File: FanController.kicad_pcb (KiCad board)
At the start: 2 copper layers, 80 x 45 mm, 28 parts, among them J1 Conn_01x02_Female, J2 Conn_01x03_Male, J3 Conn_01x03_Male, J4 Conn_01x03_Male, J5 Conn_01x03_Male, Q1 AO3400A, Q2 AO3400A, Q3 AO3400A, Q4 AO3400A, U1 D-SUN-MP1584EN, U2 mh-et-live-minikit

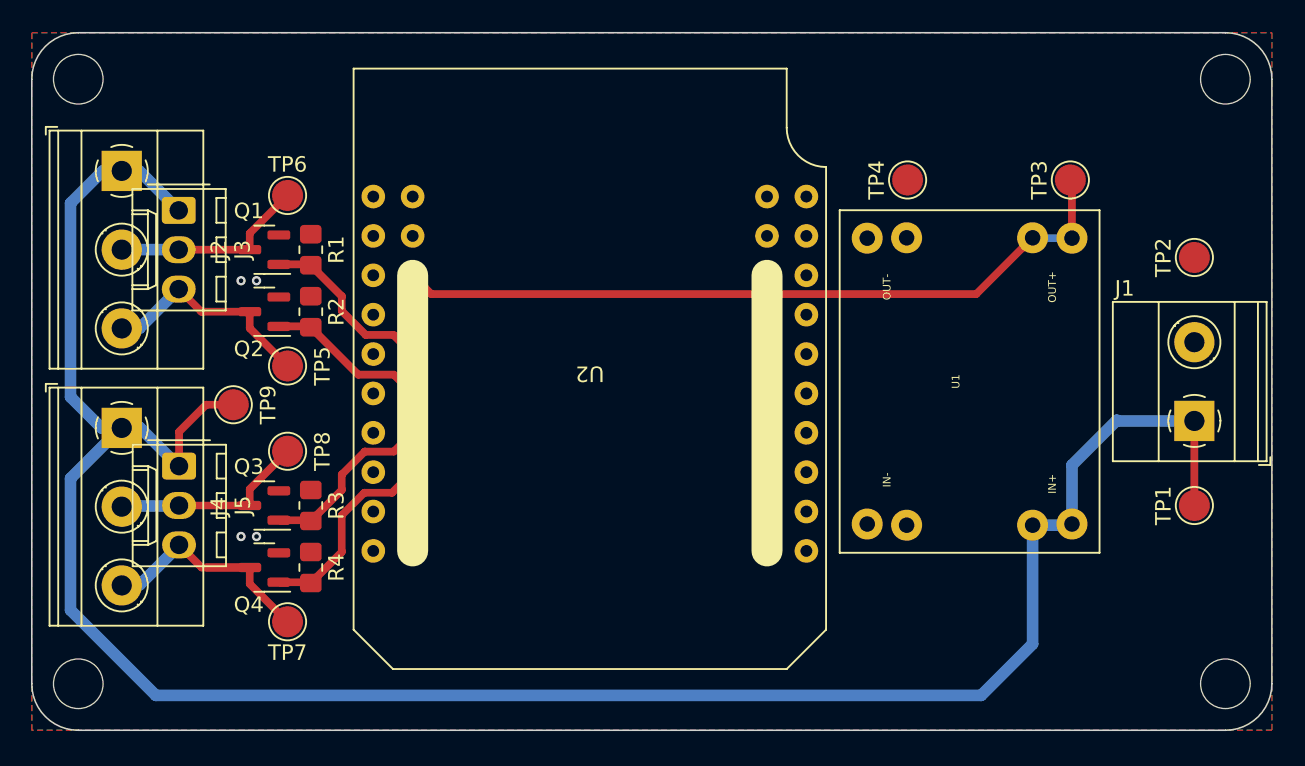
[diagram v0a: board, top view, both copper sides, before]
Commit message: shrinked board
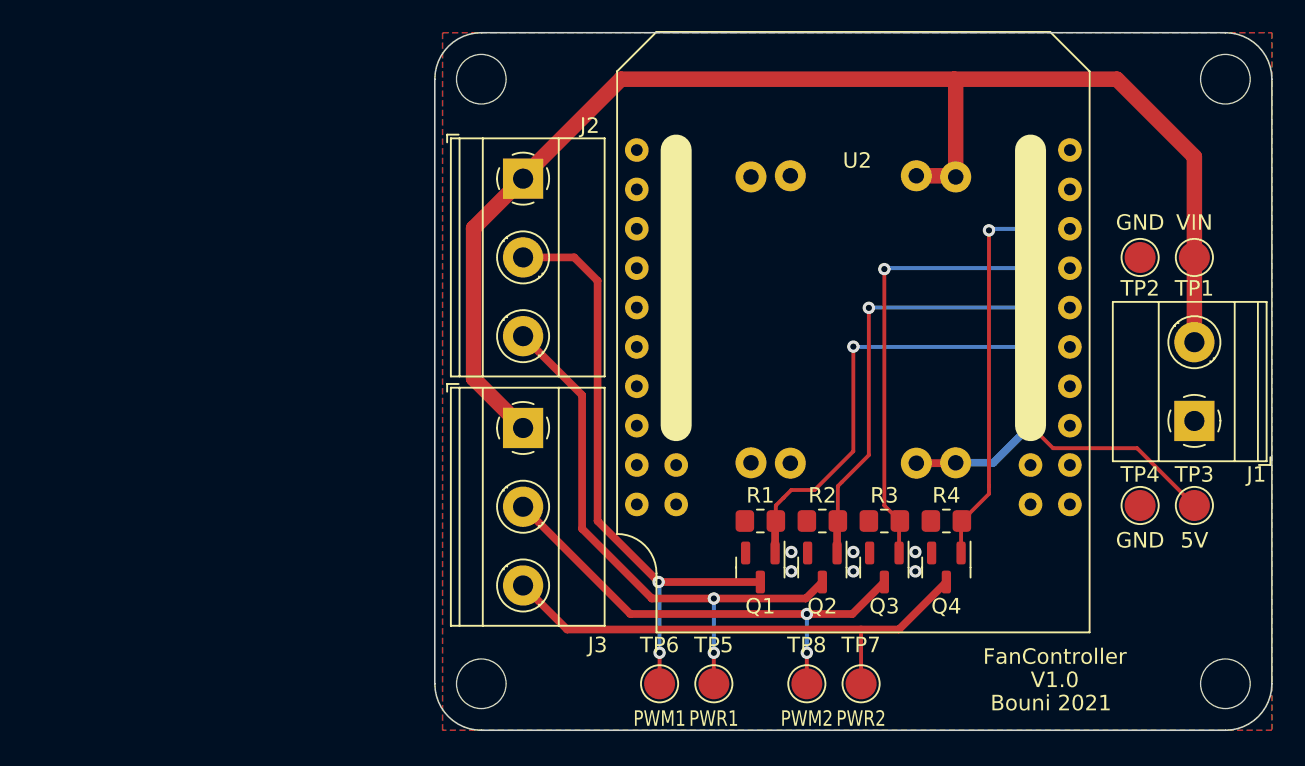
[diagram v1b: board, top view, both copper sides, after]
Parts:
- removed the J3 at (49.5, 41.5)
- removed J5: Conn_01x03_Male, Connector_Molex:Molex_KK-254_AE-6410-03A_1x03_P2.54mm_Vertical
- removed TP9: TestPoint, TestPoint:TestPoint_Pad_D2.0mm
- U1: moved to B.Cu
- moved Q4 44.0 mm to (99.0, 64.5), turned to -90 degrees
- moved R4 41.1 mm to (99.0, 61.5), turned to 0 degrees
- moved Q3 40.2 mm to (95.0, 64.5), turned to -90 degrees
- moved Q2 39.6 mm to (91.0, 64.5), turned to -90 degrees
- moved TP6 39.6 mm to (80.5, 72.0), turned to 180 degrees
- moved Q1 38.0 mm to (87.0, 64.5), turned to -90 degrees
- moved TP7 37.2 mm to (93.5, 72.0)
- moved R3 37.0 mm to (95.0, 61.5), turned to 0 degrees
- moved TP8 36.7 mm to (90.0, 72.0), turned to -90 degrees
- moved R2 35.7 mm to (91.0, 61.5), turned to 0 degrees
- moved TP5 34.3 mm to (84.0, 72.0), turned to 90 degrees
- moved R1 33.9 mm to (87.0, 61.5), turned to 0 degrees
- moved H1 26.0 mm to (69.0, 72.0)
- moved H2 26.0 mm to (69.0, 33.0)
- moved J2 25.9 mm to (71.7, 39.4)
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- renumbered J4 to J3
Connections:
- J1 pad 1: +12V -> GND
- J1 pad 2: GND -> +12V
- U2 pad 10: unconnected-(U2-Pad10) -> (no net)
- U2 pad 11: unconnected-(U2-Pad11) -> (no net)
- U2 pad 12: unconnected-(U2-Pad12) -> (no net)
- U2 pad 13: unconnected-(U2-Pad13) -> (no net)
- U2 pad 14: unconnected-(U2-Pad14) -> (no net)
- U2 pad 15: unconnected-(U2-Pad15) -> (no net)
- U2 pad 16: unconnected-(U2-Pad16) -> (no net)
- U2 pad 17: unconnected-(U2-Pad17) -> (no net)
- U2 pad 18: unconnected-(U2-Pad18) -> (no net)
- U2 pad 19: unconnected-(U2-Pad19) -> (no net)
- U2 pad 2: unconnected-(U2-Pad2) -> (no net)
- U2 pad 20: unconnected-(U2-Pad20) -> (no net)
- U2 pad 21: unconnected-(U2-Pad21) -> (no net)
- U2 pad 22: unconnected-(U2-Pad22) -> (no net)
- U2 pad 29: unconnected-(U2-Pad29) -> (no net)
- U2 pad 3: unconnected-(U2-Pad3) -> (no net)
- U2 pad 30: unconnected-(U2-Pad30) -> (no net)
- U2 pad 32: unconnected-(U2-Pad32) -> (no net)
- U2 pad 33: unconnected-(U2-Pad33) -> (no net)
- U2 pad 34: unconnected-(U2-Pad34) -> (no net)
- U2 pad 35: unconnected-(U2-Pad35) -> (no net)
- U2 pad 36: unconnected-(U2-Pad36) -> (no net)
- U2 pad 37: unconnected-(U2-Pad37) -> (no net)
- U2 pad 38: unconnected-(U2-Pad38) -> (no net)
- U2 pad 39: unconnected-(U2-Pad39) -> (no net)
- U2 pad 4: unconnected-(U2-Pad4) -> (no net)
- U2 pad 40: unconnected-(U2-Pad40) -> (no net)
- U2 pad 5: unconnected-(U2-Pad5) -> (no net)
- U2 pad 6: unconnected-(U2-Pad6) -> (no net)
- U2 pad 7: unconnected-(U2-Pad7) -> (no net)
- U2 pad 8: unconnected-(U2-Pad8) -> (no net)
- U2 pad 9: unconnected-(U2-Pad9) -> (no net)
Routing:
- net +12V: track 144.2 -> 87.7 mm
- net +5V: track 48.3 -> 21.1 mm
- net PWR1: track 12.8 -> 39.6 mm, vias 0 -> 2
- net FAN1: track 14.4 -> 37.3 mm, vias 0 -> 2
- net PWR2: track 12.7 -> 31.5 mm, vias 0 -> 2
- net PWM1: track 10.4 -> 27.1 mm, vias 0 -> 1
- net OUT2: track 11.6 -> 28.2 mm, vias 0 -> 1
- net OUT1: track 11.6 -> 27.7 mm, vias 0 -> 1
- net FAN2: track 17.2 -> 33.2 mm
- net PWM2: track 13.0 -> 24.3 mm, vias 0 -> 1
- net GND: vias 4 -> 6
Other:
- board size 80 x 45 mm -> 54 x 45 mm
- board text added: "+"
- board text added: "-"
- board text added: "5V"
- board text added: "Bouni 2021"
- board text added: "FAN1"
- board text added: "FAN2"
- board text added: "FanController"
- board text added: "GND"
- board text added: "PWM"
- board text added: "PWM1"
- board text added: "PWM2"
- board text added: "PWR1"
- board text added: "PWR2"
- board text added: "V1.0"
- board text added: "VIN"
- board text added: "~"
- board text removed: "Labels hinzufügen!"

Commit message: minor cleanups
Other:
- board text added: "Adjust 5VDC output before connecting ESP32 board!"
- board text added: "IN+"
- board text added: "IN-"
- board text added: "MH-ET LIVE MiniKit"
- board text added: "OUT+"
- board text added: "OUT-"
- board text added: "POWER 24VDC max."
